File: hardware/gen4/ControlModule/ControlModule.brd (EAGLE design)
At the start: 100 x 80 mm, 43 parts, among them IC1 XMEGA16A4A

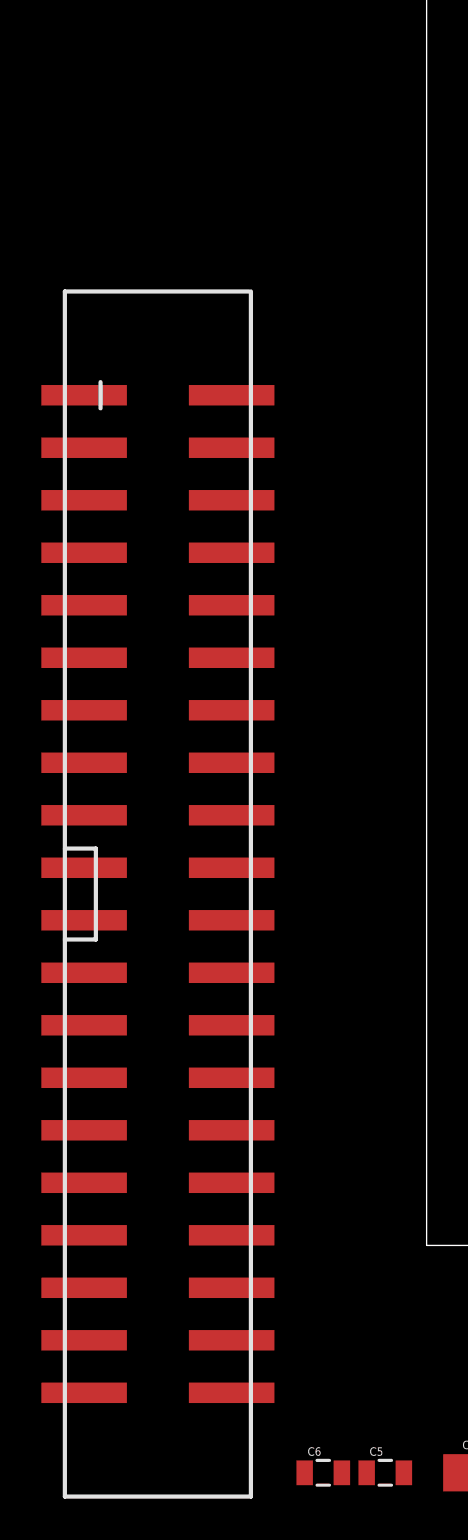
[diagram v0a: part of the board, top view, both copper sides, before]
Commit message: fix consistency error
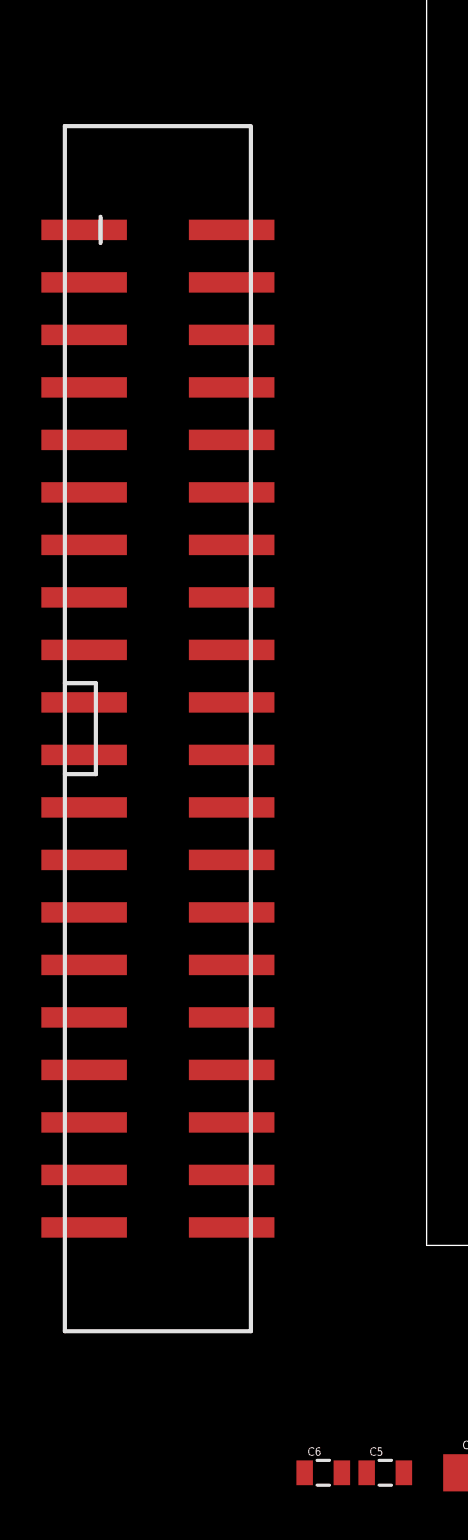
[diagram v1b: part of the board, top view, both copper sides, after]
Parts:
- moved JP1 8.00 mm to (-13.0, 25.0)
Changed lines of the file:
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@@
 <element name="C5" library="SparkFun-Capacitors" package="0805" value="1uF" x="-2" y="-11"/>
 <element name="C6" library="SparkFun-Capacitors" package="0805" value=".01uF" x="-5" y="-11"/>
-<element name="JP1" library="SparkFun-Connectors" package="2X20_SHROUDED_SMT" value="M20X2SHROUDED_SMT" x="-13" y="17"/>
+<element name="JP1" library="SparkFun-Connectors" package="2X20_SHROUDED_SMT" value="M20X2SHROUDED_SMT" x="-13" y="25"/>
 </elements>
 <signals>

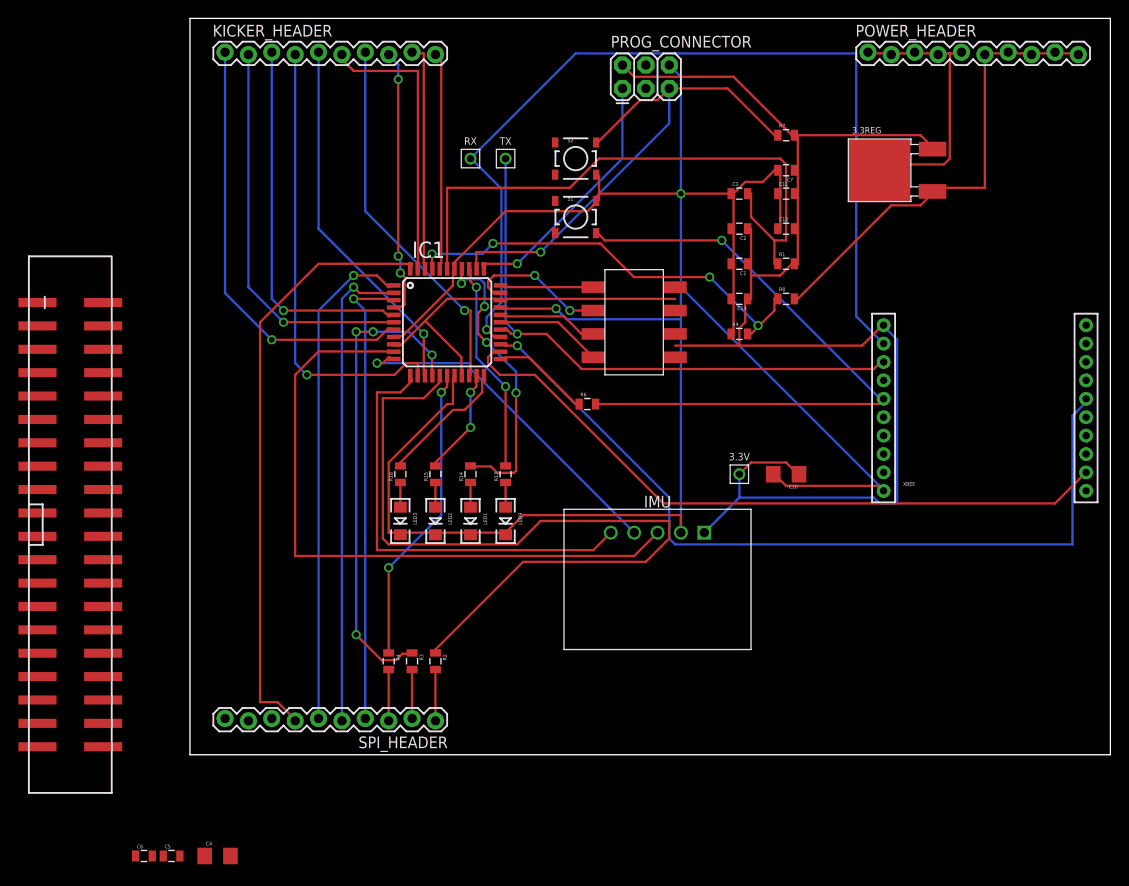
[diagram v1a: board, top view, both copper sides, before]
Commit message: updated connectors
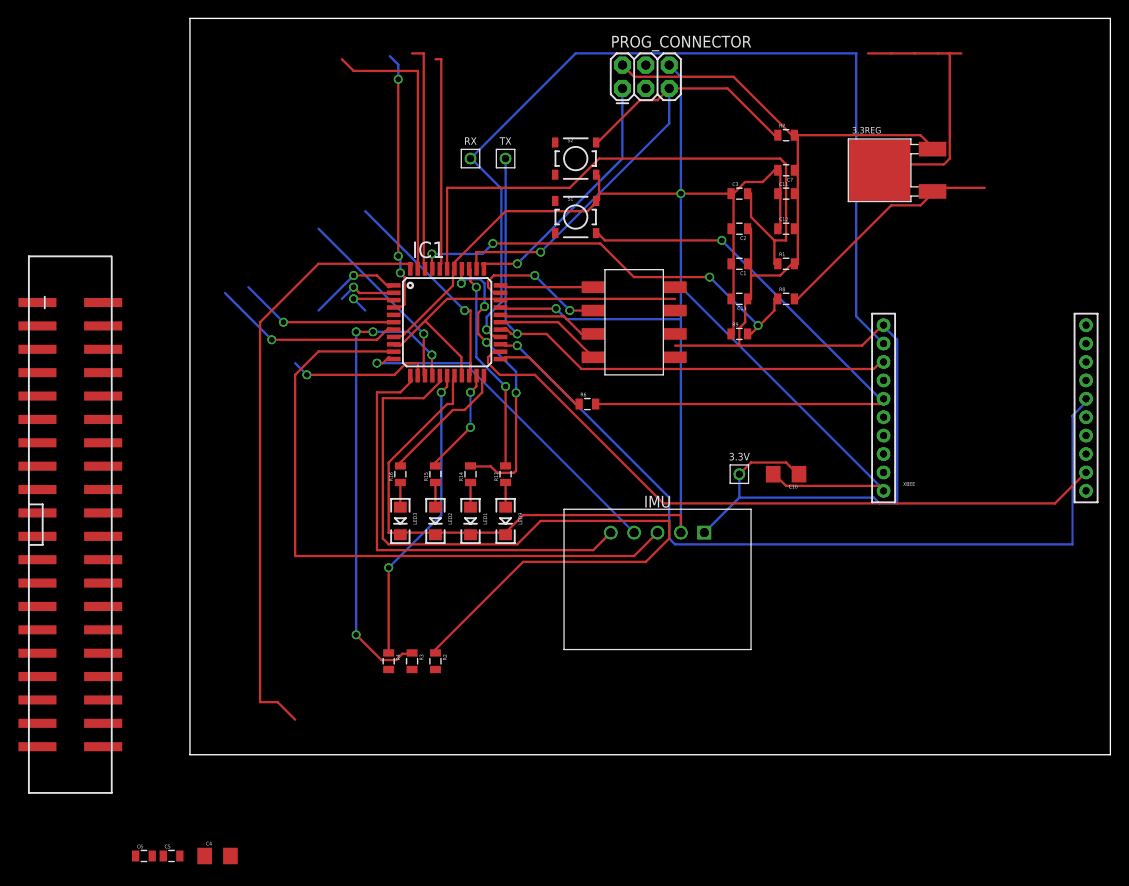
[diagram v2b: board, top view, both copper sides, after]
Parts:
- removed KICKER_HEADER, POWER_HEADER, SPI_HEADER: M10LOCK, SparkFun-Connectors:1X10_LOCK
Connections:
- removed net DONE: IC1.5, KICKER_HEADER.3
- new net CHARGE_DONE: IC1.5
- net 12V: now also JP1.1, JP1.2, JP1.3, JP1.4, JP1.5, JP1.6; no longer POWER_HEADER.10, POWER_HEADER.6, POWER_HEADER.7, POWER_HEADER.8, POWER_HEADER.9
- net 12VGND: now also JP1.35, JP1.36, JP1.37, JP1.38, JP1.39, JP1.40; no longer POWER_HEADER.1, POWER_HEADER.2, POWER_HEADER.3, POWER_HEADER.4, POWER_HEADER.5
- net BB_IN: no longer KICKER_HEADER.10
- net BB_OUT: no longer KICKER_HEADER.8
- net CHARGE: no longer KICKER_HEADER.1
- net CHIP_ENABLE: no longer KICKER_HEADER.4
- net DISCHARGE: no longer KICKER_HEADER.2
- net DIVCAP: no longer KICKER_HEADER.9
- net DRIB: no longer KICKER_HEADER.6
- net GND: now also JP1.33, JP1.34
- net KICK_ENABLE: no longer KICKER_HEADER.5
- net KICK_REF: no longer KICKER_HEADER.7
- net N$6: no longer SPI_HEADER.1
- net N$7: no longer SPI_HEADER.2
- net N$8: no longer SPI_HEADER.3
- net SS_1: no longer SPI_HEADER.4
- net SS_2: no longer SPI_HEADER.5
- net SS_3: no longer SPI_HEADER.6
- net SS_4: no longer SPI_HEADER.7
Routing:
- net SS_2: track 52.3 -> 6.42 mm
- net SS_3: track 54.6 -> 10.3 mm
- net SS_1: track 50.5 -> 6.17 mm
- net DONE: track 40.9 -> 0.00 mm, vias 1 -> 0
- net CHIP_ENABLE: track 49.3 -> 15.7 mm
- net CHARGE: track 47.1 -> 21.0 mm
- net 12V: track 51.0 -> 25.8 mm
- net DISCHARGE: track 42.6 -> 17.4 mm
- net KICK_ENABLE: track 40.0 -> 20.8 mm
- net KICK_REF: track 40.3 -> 23.1 mm
- net N$8: track 5.58 -> 0.00 mm
- net N$6: track 5.58 -> 0.00 mm
- net N$7: track 5.32 -> 0.00 mm
- net 12VGND: track 30.4 -> 29.7 mm
- net DRIB: track 30.8 -> 30.3 mm
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
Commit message: added new discharge circuit - spruced up for design review
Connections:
- net BB_IN: now also JP1.7
- net BB_OUT: now also JP1.9
- net CHARGE: now also JP1.19
- net CHARGE_DONE: now also JP1.17
- net CHIP_ENABLE: now also JP1.13
- net DISCHARGE: now also JP1.16
- net DIVCAP: now also JP1.14
- net DRIB: now also JP1.18
- net KICK_ENABLE: now also JP1.11
- net KICK_REF: now also JP1.15
- net N$6: now also JP1.30
- net N$7: now also JP1.32
- net N$8: now also JP1.28
- net SS_1: now also JP1.20
- net SS_2: now also JP1.22
- net SS_3: now also JP1.24
- net SS_4: now also JP1.26
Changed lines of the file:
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@@
 <wire x1="26.67" y1="75.565" x2="27.305" y2="75.565" width="0.254" layer="1"/>
 <wire x1="27.305" y1="53.34" x2="27.14" y2="52.79" width="0.254" layer="1"/>
+<contactref element="JP1" pad="7"/>
+<wire x1="-16.5687" y1="41.51" x2="27.14" y2="52.79" width="0" layer="19" extent="1-1"/>
 </signal>
 <signal name="BATSENSE">
@@
 <wire x1="24.13" y1="76.2" x2="25.4" y2="76.2" width="0.254" layer="1"/>
 <wire x1="25.4" y1="53.34" x2="25.54" y2="52.79" width="0.254" layer="1"/>
+<contactref element="JP1" pad="14"/>
+<wire x1="-9.4313" y1="33.89" x2="25.54" y2="52.79" width="0" layer="19" extent="1-1"/>
 </signal>
 <signal name="RESET">
@@
 <wire x1="30.48" y1="41.275" x2="30.34" y2="41.19" width="0.254" layer="1"/>
 <via x="29.845" y="48.26" extent="1-16" drill="0.6096"/>
+<contactref element="JP1" pad="15"/>
+<wire x1="-16.5687" y1="31.35" x2="19.05" y2="59.055" width="0" layer="19" extent="1-16"/>
 </signal>
 <signal name="N$5">
@@
 <via x="22.6314" y="54.1782" extent="1-16" drill="0.6096"/>
 <via x="22.6314" y="73.3806" extent="1-16" drill="0.6096"/>
+<contactref element="JP1" pad="9"/>
+<wire x1="-16.5687" y1="38.97" x2="22.14" y2="48.59" width="0" layer="19" extent="1-1"/>
 </signal>
 <signal name="RTS">
@@
 <signal name="N$6">
 <contactref element="R2" pad="2"/>
+<contactref element="JP1" pad="30"/>
+<wire x1="-9.4313" y1="13.57" x2="26.67" y2="9.26" width="0" layer="19" extent="1-1"/>
 </signal>
 <signal name="N$7">
 <contactref element="R3" pad="2"/>
+<contactref element="JP1" pad="32"/>
+<wire x1="-9.4313" y1="11.03" x2="24.13" y2="9.26" width="0" layer="19" extent="1-1"/>
 </signal>
 <signal name="N$8">
 <contactref element="R4" pad="2"/>
+<contactref element="JP1" pad="28"/>
+<wire x1="-9.4313" y1="16.11" x2="21.59" y2="9.26" width="0" layer="19" extent="1-1"/>
 </signal>
 <signal name="DISCHARGE">
@@
 <wire x1="6.35" y1="50.8" x2="10.16" y2="46.99" width="0.254" layer="16"/>
 <via x="10.16" y="46.99" extent="1-16" drill="0.6096"/>
+<contactref element="JP1" pad="16"/>
+<wire x1="-9.4313" y1="31.35" x2="6.35" y2="50.8" width="0" layer="19" extent="1-16"/>
 </signal>
 <signal name="DRIB">
@@
 <wire x1="16.51" y1="75.565" x2="17.78" y2="74.295" width="0.254" layer="1"/>
 <wire x1="24.765" y1="53.34" x2="24.74" y2="52.79" width="0.254" layer="1"/>
+<contactref element="JP1" pad="18"/>
+<wire x1="-9.4313" y1="28.81" x2="24.74" y2="52.79" width="0" layer="19" extent="1-1"/>
 </signal>
 <signal name="GLED1">
@@
 <wire x1="21.59" y1="46.355" x2="22.14" y2="46.19" width="0.254" layer="1"/>
 <via x="8.89" y="45.085" extent="1-16" drill="0.6096"/>
+<contactref element="JP1" pad="19"/>
+<wire x1="-16.5687" y1="26.27" x2="3.81" y2="50.165" width="0" layer="19" extent="1-16"/>
 </signal>
 <signal name="CHIP_ENABLE">
@@
 <wire x1="24.765" y1="41.275" x2="24.74" y2="41.19" width="0.254" layer="1"/>
 <via x="12.7" y="41.275" extent="1-16" drill="0.6096"/>
+<contactref element="JP1" pad="13"/>
+<wire x1="-16.5687" y1="33.89" x2="11.43" y2="42.545" width="0" layer="19" extent="1-16"/>
 </signal>
 <signal name="KICK_ENABLE">
@@
 <wire x1="25.4" y1="41.275" x2="25.54" y2="41.19" width="0.254" layer="1"/>
 <via x="25.4" y="45.72" extent="1-16" drill="0.6096"/>
+<contactref element="JP1" pad="11"/>
+<wire x1="-16.5687" y1="36.43" x2="13.97" y2="57.15" width="0" layer="19" extent="1-16"/>
 </signal>
 <signal name="SS_3">
@@
 <wire x1="21.59" y1="50.8" x2="22.14" y2="50.99" width="0.254" layer="1"/>
 <via x="17.78" y="52.07" extent="1-16" drill="0.6096"/>
+<contactref element="JP1" pad="24"/>
+<wire x1="-9.4313" y1="21.19" x2="13.97" y2="48.26" width="0" layer="19" extent="1-16"/>
 </signal>
 <signal name="SS_2">
@@
 <wire x1="21.59" y1="50.165" x2="22.14" y2="50.19" width="0.254" layer="1"/>
 <via x="17.78" y="50.8" extent="1-16" drill="0.6096"/>
+<contactref element="JP1" pad="22"/>
+<wire x1="-9.4313" y1="23.73" x2="16.51" y2="49.53" width="0" layer="19" extent="1-16"/>
 </signal>
 <signal name="SS_1">
@@
 <wire x1="21.59" y1="49.53" x2="22.14" y2="49.39" width="0.254" layer="1"/>
 <via x="17.78" y="49.53" extent="1-16" drill="0.6096"/>
+<contactref element="JP1" pad="20"/>
+<wire x1="-9.4313" y1="26.27" x2="17.78" y2="49.53" width="0" layer="19" extent="1-1"/>
 </signal>
 <signal name="SS_4">
@@
 <wire x1="11.43" y1="3.81" x2="9.525" y2="5.715" width="0.254" layer="1"/>
 <wire x1="24.13" y1="53.34" x2="23.94" y2="52.79" width="0.254" layer="1"/>
+<contactref element="JP1" pad="26"/>
+<wire x1="-9.4313" y1="18.65" x2="7.62" y2="5.715" width="0" layer="19" extent="1-1"/>
 </signal>
 <signal name="CHARGE_DONE">
 <contactref element="IC1" pad="5"/>
+<contactref element="JP1" pad="17"/>
+<wire x1="-16.5687" y1="28.81" x2="22.14" y2="47.79" width="0" layer="19" extent="1-1"/>
 </signal>
 </signals>

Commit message: comms board done - needs review
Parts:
- moved FRAME1 134.0 mm to (-78.7, 81.3)
- moved C5 74.1 mm to (18.7, 60.2), turned to 90 degrees
- moved C6 74.1 mm to (15.5, 60.2), turned to 90 degrees
- moved 3.3REG 69.6 mm to (5.33, 61.4)
- moved 3.3V 68.7 mm to (3.90, 70.5)
- moved C4 66.2 mm to (6.60, 55.1), turned to 180 degrees
- moved PROG_CONNECTOR 61.2 mm to (57.9, 12.2), turned to 180 degrees
- moved C7 60.0 mm to (77.0, 4.79), turned to 0 degrees
- moved S2 57.7 mm to (74.2, 17.0), turned to 180 degrees
- moved C11 55.6 mm to (73.4, 6.06)
- moved R7 55.3 mm to (71.6, 12.4), turned to 270 degrees
- moved XBEE 55.0 mm to (48.5, 66.5), turned to 180 degrees
- moved C3 52.0 mm to (78.2, 12.4), turned to 90 degrees
- moved LED9 51.4 mm to (12.1, 71.7)
- moved C12 51.3 mm to (77.0, 7.33), turned to 180 degrees
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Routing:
- net GND: track 248.0 -> 45.9 mm, vias 2 -> 4
- net RLED2: track 14.3 -> 153.3 mm, vias 0 -> 4
- net GLED2: track 11.7 -> 137.3 mm, vias 2 -> 4
- net MOSI: track 88.1 -> 6.18 mm
- net CHIP_ENABLE: track 15.7 -> 92.9 mm, vias 1 -> 3
- net KICK_ENABLE: track 20.8 -> 95.0 mm, vias 1 -> 3
- net RX: track 101.9 -> 36.1 mm
- net 12VGND: track 29.7 -> 86.5 mm, vias 0 -> 1
- net GLED1: track 23.1 -> 79.2 mm
- net RTS: track 90.1 -> 36.7 mm
- net SCL: track 38.1 -> 85.6 mm
- net KICK_REF: track 23.1 -> 69.9 mm, vias 1 -> 3
- net N$8: track 0.00 -> 45.6 mm, vias 0 -> 1
- net MISO: track 52.0 -> 6.64 mm, vias 4 -> 0
- net SS_3: track 10.3 -> 51.0 mm, vias 1 -> 5
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- added copper zone on layer 1, net GND
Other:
- board size 100 x 80 mm -> 96.7 x 75.3 mm

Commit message: almost done with shrinking comms board but computer is at 2 percent and I dont have a charger :/
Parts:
- removed IMU: MPU6050IMUMPU, gen3:MPU-6050IMU
- moved 3.3V 85.1 mm to (57.0, 4.02)
- moved LED9 74.6 mm to (62.6, 16.8), turned to 0 degrees
- moved R13 74.0 mm to (62.4, 20.0), turned to 0 degrees
- moved C5 66.4 mm to (53.0, 3.34), turned to 270 degrees
- moved C6 65.9 mm to (48.8, 3.34), turned to 270 degrees
- moved LED3 65.2 mm to (62.8, 23.5), turned to 0 degrees
- moved R16 64.9 mm to (62.6, 26.7), turned to 0 degrees
- moved 3.3REG 63.6 mm to (48.3, 14.6), turned to 270 degrees
- moved C4 63.2 mm to (42.9, 3.38)
- moved LED2 55.8 mm to (62.7, 29.8), turned to 0 degrees
- moved R15 55.2 mm to (62.4, 33.3), turned to 0 degrees
- moved LED1 46.4 mm to (62.7, 36.4), turned to 0 degrees
- moved C3 46.4 mm to (32.7, 3.73), turned to 180 degrees
- moved R14 46.3 mm to (62.7, 39.3), turned to 0 degrees
- moved C12 44.5 mm to (32.6, 11.5), turned to 0 degrees
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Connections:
- net 3.3V: no longer IMU.VCC
- net GND: no longer IMU.GND
- net INT: no longer IMU.INT
- net SCL: no longer IMU.SCL
- net SDA: no longer IMU.SDA
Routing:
- net RLED2: track 153.3 -> 31.3 mm, vias 4 -> 0
- net GLED2: track 137.3 -> 19.8 mm, vias 4 -> 0
- net 3.3V: track 201.4 -> 88.9 mm
- net SDA: track 99.0 -> 0.00 mm, vias 1 -> 0
- net SCL: track 85.6 -> 0.00 mm, vias 1 -> 0
- net KICK_ENABLE: track 95.0 -> 19.1 mm
- net CHIP_ENABLE: track 92.9 -> 19.9 mm
- net INT: track 70.9 -> 0.00 mm, vias 1 -> 0
- net KICK_REF: track 69.9 -> 4.20 mm, vias 3 -> 1
- net N$1: track 53.7 -> 2.70 mm, vias 2 -> 0
- net SS_3: track 51.0 -> 0.00 mm, vias 5 -> 0
- net DRIB: track 42.1 -> 0.00 mm, vias 3 -> 0
- net N$8: track 45.6 -> 7.66 mm
- net SS_2: track 39.7 -> 3.57 mm, vias 3 -> 1
- net 12VGND: track 86.5 -> 50.5 mm, vias 1 -> 3
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- added copper zone on layer 16, net GND
- removed copper zone on layer 1, net GND
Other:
- board size 96.7 x 75.3 mm -> 48.1 x 75.1 mm
